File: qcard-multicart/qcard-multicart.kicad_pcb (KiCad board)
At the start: 2 copper layers, 55 x 46.5 mm, 13 parts, among them J1 Conn_02x18_Top_Bottom, SW1 SW_DIP_x04, U1 MX29LV640EBTI-70G, U2 MIC5365-3.3YD5

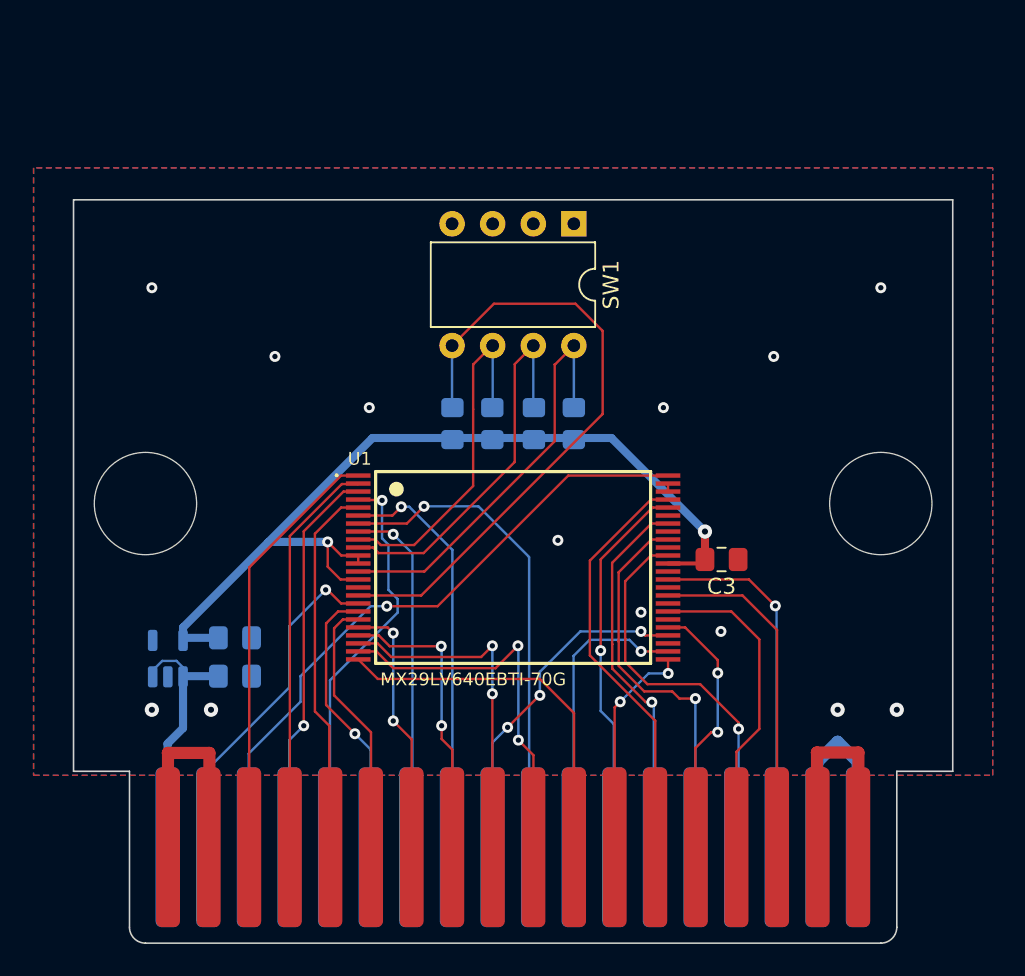
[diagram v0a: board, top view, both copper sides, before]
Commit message: Adding 4mm clearance to switches
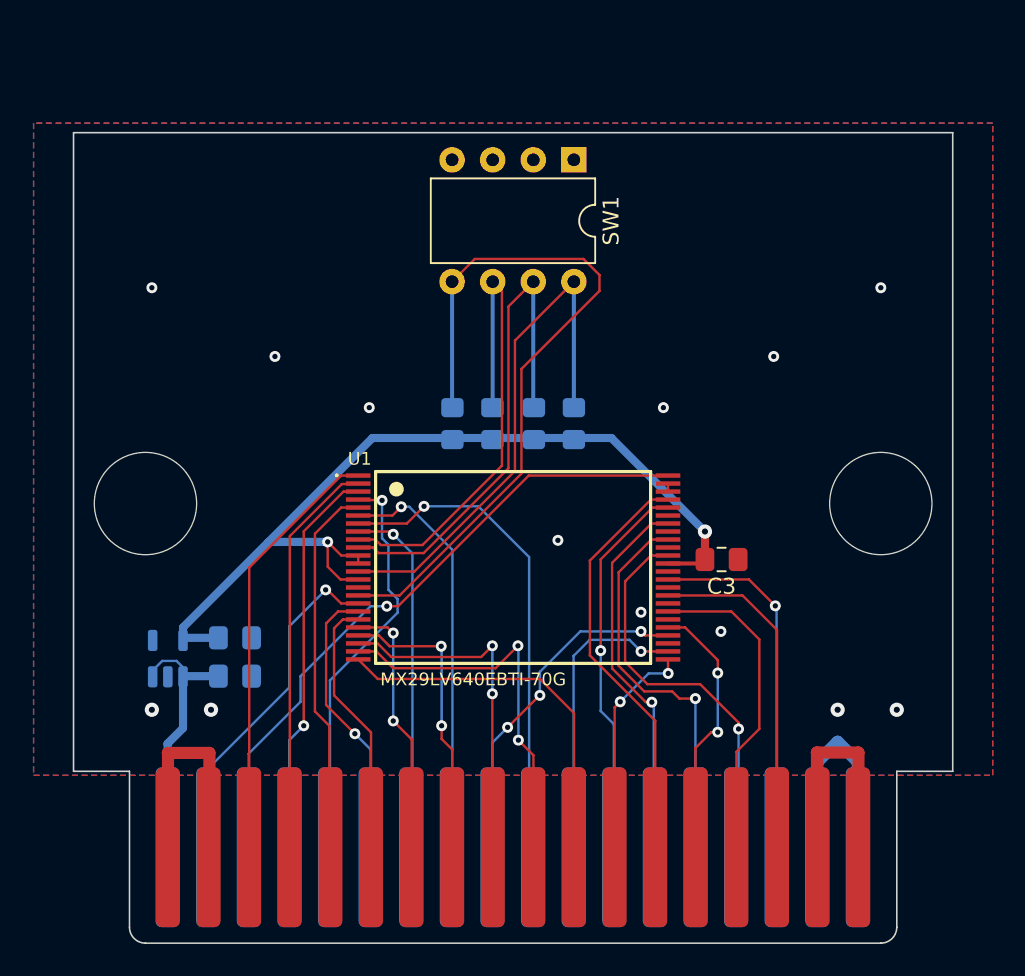
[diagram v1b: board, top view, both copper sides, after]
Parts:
- moved SW1 4.00 mm to (100.8, 32.5)
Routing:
- net Net-(U1-A19): track 22.0 -> 30.8 mm
- net Net-(U1-A20): track 23.9 -> 32.0 mm
- net Net-(U1-A21): track 26.0 -> 33.7 mm
- net Net-(U1-A18): track 40.3 -> 45.9 mm
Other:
- board size 55 x 46.5 mm -> 55 x 50.7 mm

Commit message: Adding another 4mm clearance, cutting out dead board
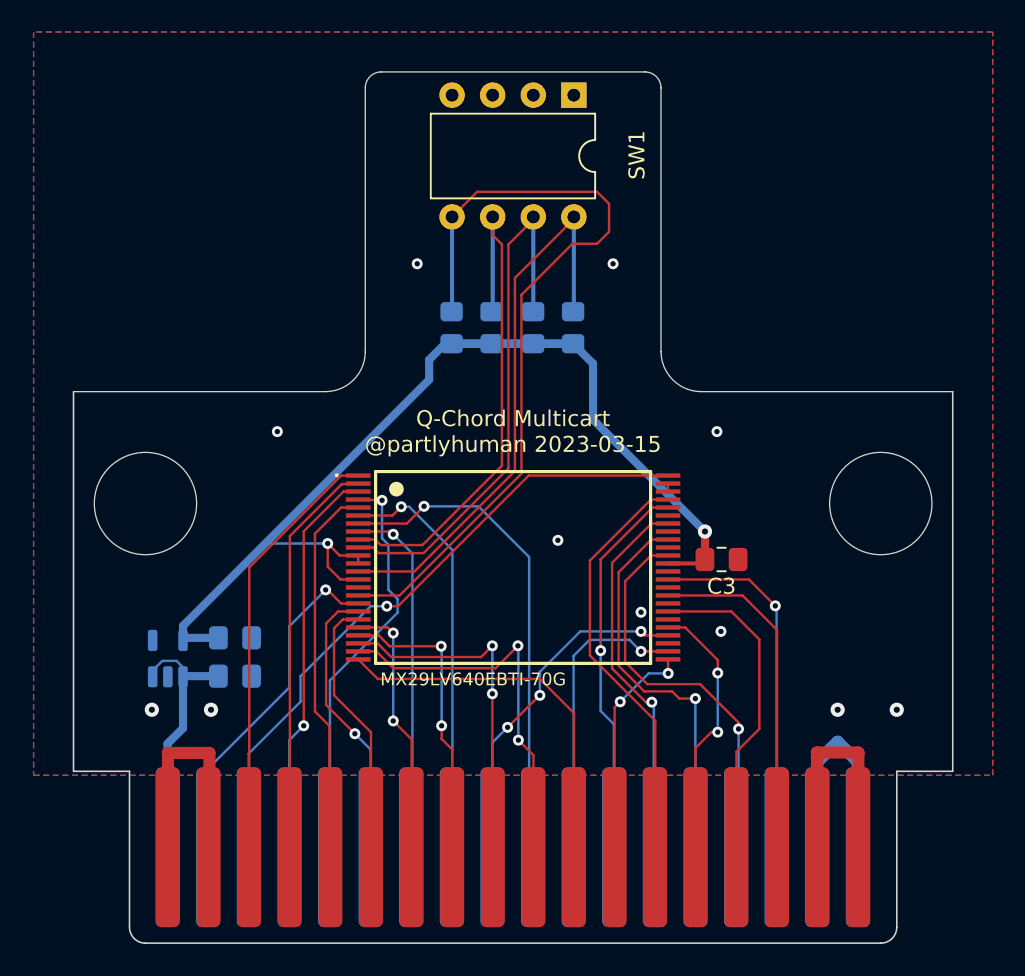
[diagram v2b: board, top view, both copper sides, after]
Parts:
- moved R1 6.00 mm to (93.2, 43.0)
- moved R2 6.00 mm to (95.7, 43.0)
- moved R3 6.00 mm to (98.2, 43.0)
- moved R4 6.00 mm to (100.8, 43.0)
- moved SW1 4.05 mm to (100.8, 28.4)
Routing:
- net +3.3V: track 57.5 -> 72.6 mm
- net Net-(U1-A18): track 45.9 -> 50.1 mm
- net Net-(U1-A21): track 33.7 -> 35.8 mm
- net Net-(U1-A19): track 30.8 -> 32.9 mm
- net Net-(U1-A20): track 32.0 -> 34.0 mm
- net GND: vias 13 -> 11
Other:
- board size 55 x 50.7 mm -> 55 x 54.5 mm

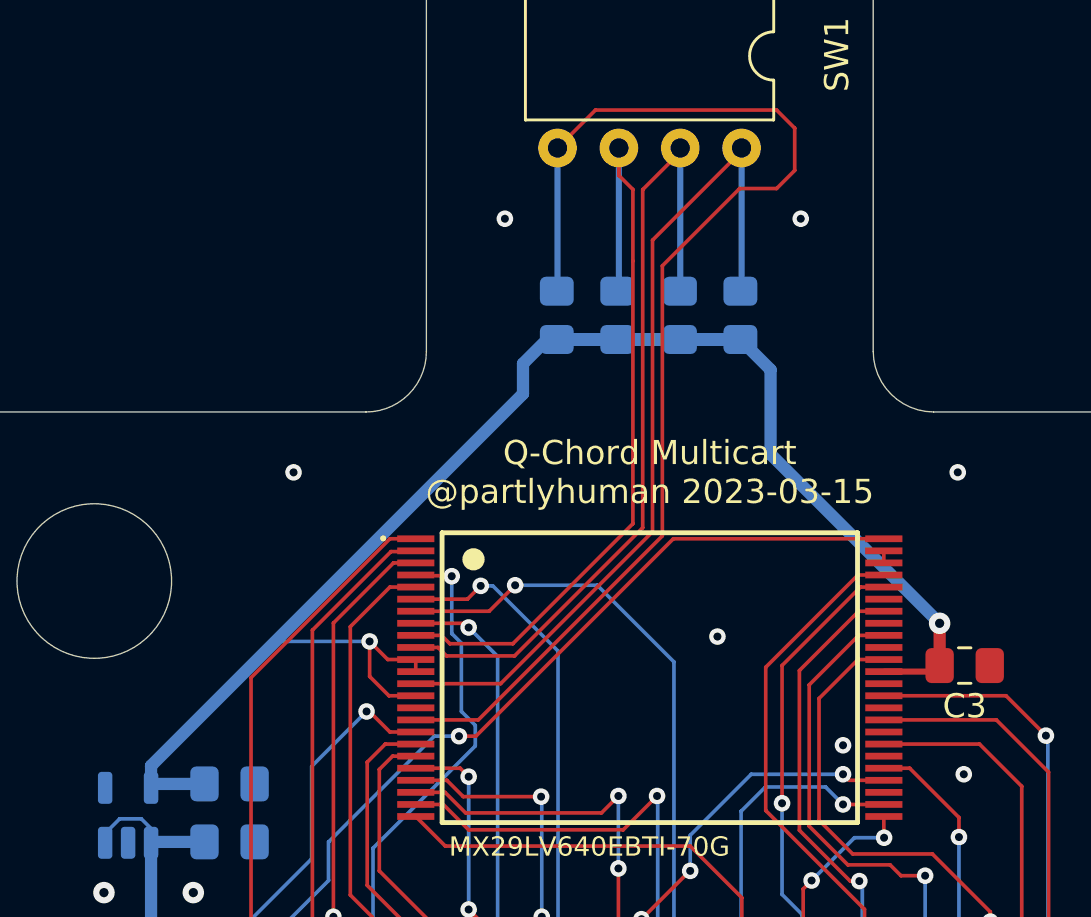
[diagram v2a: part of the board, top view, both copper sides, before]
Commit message: Refactor multicart to use SMD resistor array for ease of assembly
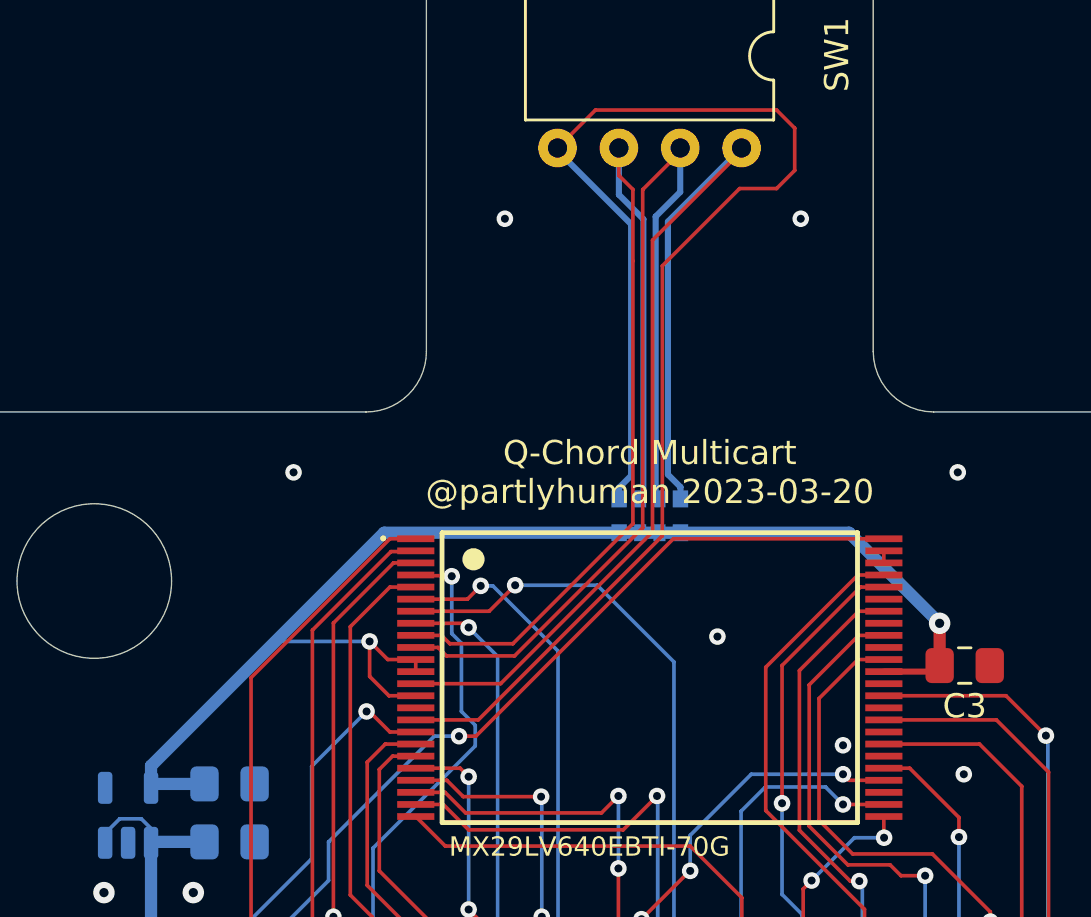
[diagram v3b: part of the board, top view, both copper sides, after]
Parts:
- removed R1, R2, R3, R4: R, Resistor_SMD:R_0805_2012Metric_Pad1.20x1.40mm_HandSolder
- added RN1: 10K, Resistor_SMD:R_Array_Convex_4x0612, B.Cu at (97.0, 51.3)
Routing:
- net +3.3V: track 72.6 -> 55.6 mm
- net Net-(RN1-R1.2): track 35.8 -> 45.8 mm
- net Net-(RN1-R4.2): track 50.1 -> 60.2 mm
- net Net-(RN1-R2.2): track 34.0 -> 43.1 mm
- net Net-(RN1-R3.2): track 32.9 -> 42.0 mm

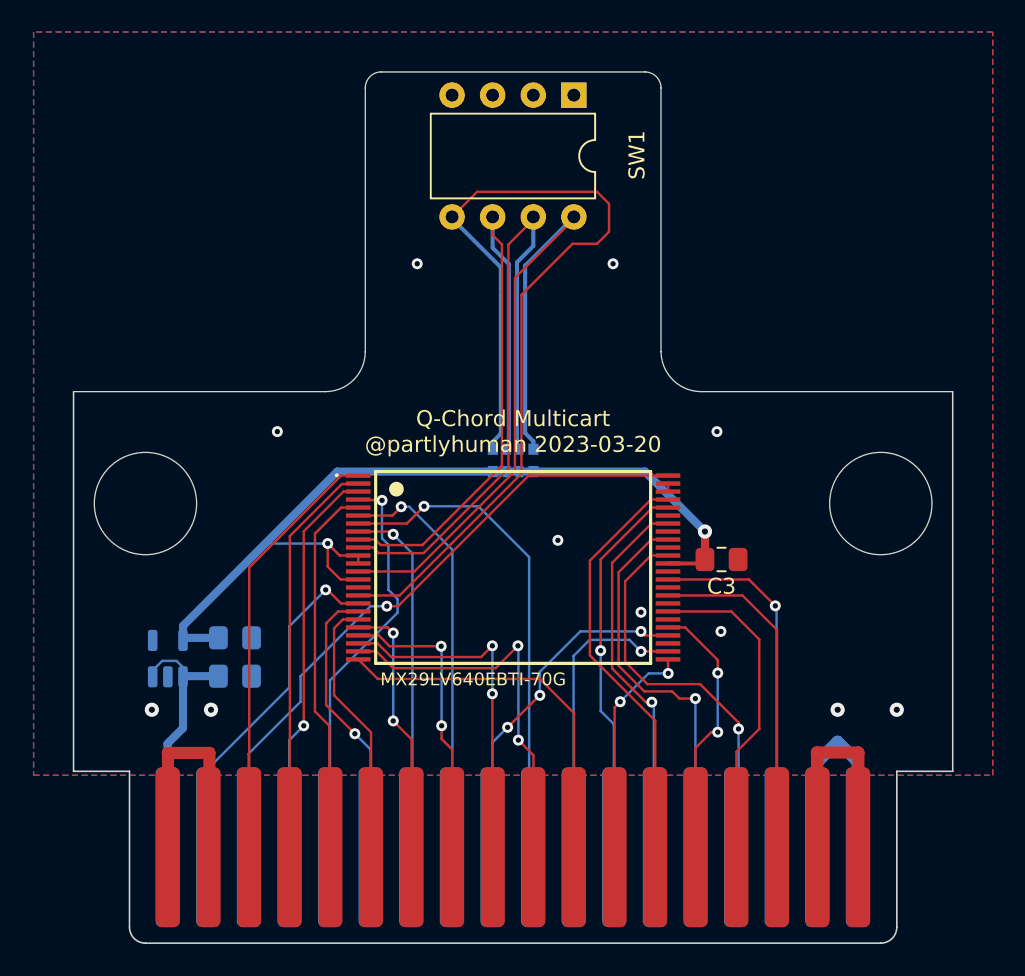
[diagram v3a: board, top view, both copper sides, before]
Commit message: Removes resistor pack, current limits pulled up inputs
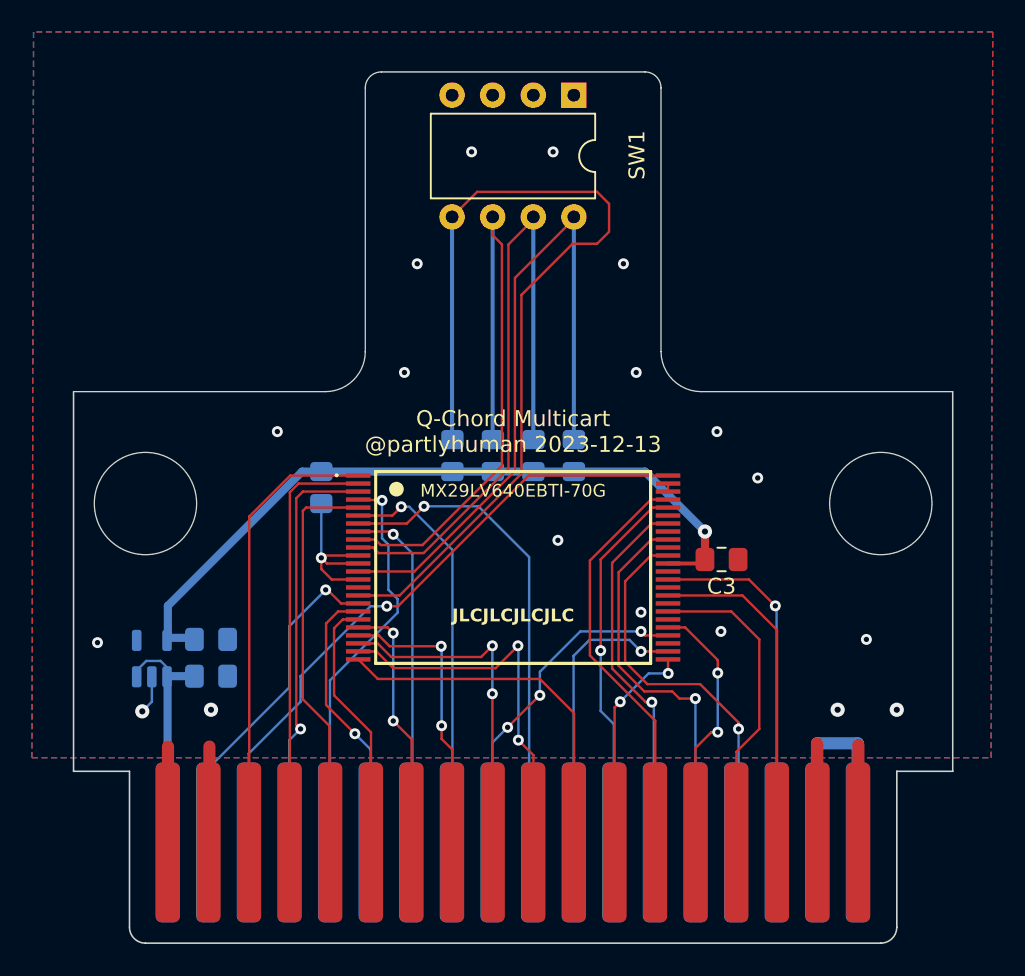
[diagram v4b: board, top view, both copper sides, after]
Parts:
- removed RN1: 10K, Resistor_SMD:R_Array_Convex_4x0612
- added R1: 10K, Resistor_SMD:R_0805_2012Metric_Pad1.20x1.40mm_HandSolder, B.Cu at (85.0, 53.0)
- added R2: 10K, Resistor_SMD:R_0805_2012Metric_Pad1.20x1.40mm_HandSolder, B.Cu at (93.2, 51.0)
- added R3: 10K, Resistor_SMD:R_0805_2012Metric_Pad1.20x1.40mm_HandSolder, B.Cu at (95.7, 51.0)
- added R4: 10K, Resistor_SMD:R_0805_2012Metric_Pad1.20x1.40mm_HandSolder, B.Cu at (98.3, 51.0)
- added R5: 10K, Resistor_SMD:R_0805_2012Metric_Pad1.20x1.40mm_HandSolder, B.Cu at (100.8, 51.0)
- C3: value 100pF -> 0.1uF
- moved C2 1.50 mm to (78.1, 62.5)
- moved C1 1.50 mm to (78.1, 64.8)
- moved U2 1.00 mm to (74.4, 63.7)
- moved J1 0.30 mm to (97.0, 75.2)
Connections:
- U1 pad 11: +3.3V -> Net-(U1-WE#)
- U1 pad 12: +3.3V -> Net-(U1-WE#)
- U1 pad 14: +3.3V -> Net-(U1-WE#)
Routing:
- net Net-(U1-WE#): track 0.00 -> 11.5 mm, vias 0 -> 1
- net +3.3V: track 55.6 -> 46.8 mm, vias 2 -> 1
- net Net-(U1-A21): track 45.8 -> 43.8 mm
- net Net-(U1-A18): track 60.2 -> 58.1 mm
- net /A12: track 23.4 -> 25.3 mm
- net /A16: track 26.7 -> 28.6 mm
- net /A14: track 24.6 -> 26.3 mm
- net /A15: track 25.1 -> 26.7 mm
- net Net-(U1-A20): track 43.1 -> 42.0 mm
- net Net-(U1-A19): track 42.0 -> 40.9 mm
- net +5V: track 16.6 -> 15.7 mm
- net GND: track 43.6 -> 43.9 mm, vias 11 -> 18
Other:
- board text added: "JLCJLCJLCJLC"

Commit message: Move all components to front
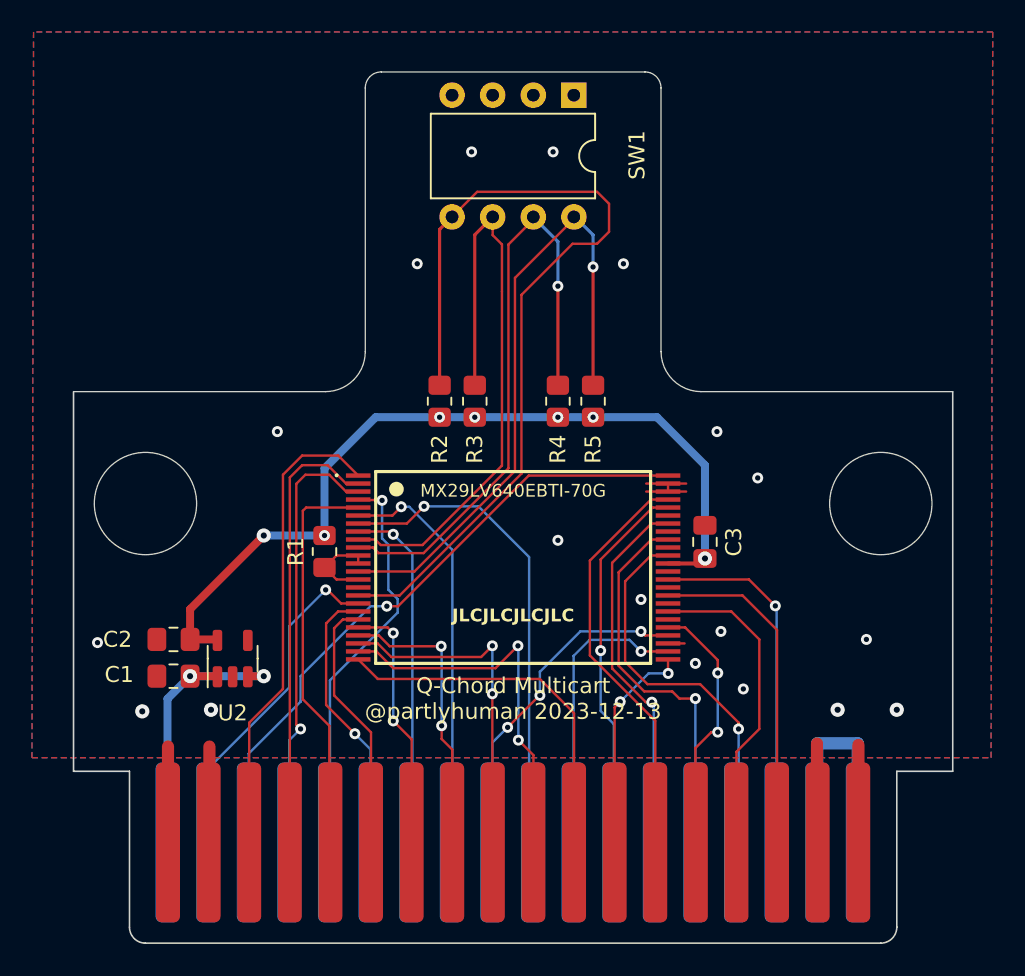
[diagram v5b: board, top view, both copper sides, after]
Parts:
- C1, C2, R2, R3, R4, R5, U2: moved to F.Cu
- R1: value 10K -> 1K; moved to F.Cu
- moved U2 5.05 mm to (79.5, 63.7)
- moved R1 4.00 mm to (85.2, 57.0)
- moved R4 3.73 mm to (99.8, 47.6)
- moved R5 3.61 mm to (102.0, 47.6)
- moved R3 3.58 mm to (94.6, 47.6)
- moved R2 3.49 mm to (92.4, 47.6)
- moved C1 2.35 mm to (75.8, 64.8), turned to 180 degrees
- moved C2 2.35 mm to (75.8, 62.5), turned to 180 degrees
- moved C3 1.51 mm to (109.0, 56.4), turned to -90 degrees
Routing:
- net Net-(U1-WE#): track 11.5 -> 5.34 mm, vias 1 -> 0
- net +3.3V: track 46.8 -> 52.8 mm, vias 1 -> 7
- net GND: track 43.9 -> 47.4 mm
- net Net-(U1-A18): track 58.1 -> 55.0 mm
- net Net-(U1-A19): track 40.9 -> 38.0 mm
- net Net-(U1-A21): track 43.8 -> 40.9 mm, vias 0 -> 1
- net Net-(U1-A20): track 42.0 -> 39.3 mm, vias 0 -> 1
- net +5V: track 15.7 -> 18.3 mm, vias 0 -> 2
- net /A15: track 26.7 -> 28.2 mm
- net /A14: track 26.3 -> 27.7 mm
- net /A16: track 28.6 -> 29.9 mm

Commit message: Production ready files
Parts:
- SW1: value SW_DIP_x04 -> 774-1954MST
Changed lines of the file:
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@@
   (title_block
     (title "Q-Chord Multicart")
-    (date "2023-12-13")
-    (rev "3")
+    (date "2024-01-13")
+    (rev "4")
     (company "@partlyhuman")
   )
@@
         (effects (font (size 1 1) (thickness 0.15)))
     )
-    (fp_text value "SW_DIP_x04" (at 3.81 9.95 90) (layer "F.Fab")
-        (effects (font (size 1 1) (thickness 0.15)))
-    )
+    (fp_text value "774-1954MST" (at 3.81 9.95 90) (layer "F.Fab")
+        (effects (font (size 1 1) (thickness 0.15)))
+    )
